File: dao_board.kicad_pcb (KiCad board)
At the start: 2 copper layers, 80 x 57 mm, 39 parts, among them J1 KEY1, J10 DISH_SENSOR, J11 5V_BOOST, J12 BATTERY, J13 DISH_LED, J2 KEY2, J3 KEY3, J4 KEY4, J5 KEY5, J6 KEY6, J7 KEY7, J8 START, J9 SELECT, SW1 SW_SPDT, SW2 HX 3x4x2-2P-1.6N, U1 XIAO-nRF52840-Plus-SMD, U2 74HC595, U3 74HC595

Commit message: 回路図を大幅に更新したのでPCBは作り直し
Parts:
- removed C1, C3, C4: 100n, PCM_Capacitor_SMD_AKL:C_0402_1005Metric
- removed C2: 10u, PCM_Capacitor_SMD_AKL:C_0603_1608Metric
- removed D1, D2: 1SS404, PCM_Diode_SMD_AKL:D_SOD-323
- removed H1, H2, H3, H4: MountingHole, PCM_fab:MountingHole_M5
- removed J1: KEY1, Connector_JST:JST_XH_B4B-XH-A_1x04_P2.50mm_Vertical
- removed J10: DISH_SENSOR, Connector_JST:JST_XH_B4B-XH-A_1x04_P2.50mm_Vertical
- removed J11: 5V_BOOST, Connector_JST:JST_XH_B4B-XH-A_1x04_P2.50mm_Vertical
- removed J12: BATTERY, Connector_JST:JST_PH_B2B-PH-K_1x02_P2.00mm_Vertical
- removed J13: DISH_LED, Connector_JST:JST_XH_B2B-XH-A_1x02_P2.50mm_Vertical
- removed J2: KEY2, Connector_JST:JST_XH_B4B-XH-A_1x04_P2.50mm_Vertical
- removed J3: KEY3, Connector_JST:JST_XH_B4B-XH-A_1x04_P2.50mm_Vertical
- removed J4: KEY4, Connector_JST:JST_XH_B4B-XH-A_1x04_P2.50mm_Vertical
- removed J5: KEY5, Connector_JST:JST_XH_B4B-XH-A_1x04_P2.50mm_Vertical
- removed J6: KEY6, Connector_JST:JST_XH_B4B-XH-A_1x04_P2.50mm_Vertical
- removed J7: KEY7, Connector_JST:JST_XH_B4B-XH-A_1x04_P2.50mm_Vertical
- removed J8: START, Connector_JST:JST_XH_B4B-XH-A_1x04_P2.50mm_Vertical
- removed J9: SELECT, Connector_JST:JST_XH_B4B-XH-A_1x04_P2.50mm_Vertical
- removed R1, R2: 1k, PCM_Resistor_SMD_AKL:R_0402_1005Metric
- removed R3, R4: 10k, PCM_Resistor_SMD_AKL:R_0402_1005Metric
- removed R5: 0, PCM_Resistor_SMD_AKL:R_0402_1005Metric
- removed SW1: SW_SPDT, IIDXtorollerparts:SW-SMD_MK-12C02-G020
- removed SW2: HX 3x4x2-2P-1.6N, IIDXtorollerparts:KEY-SMD_L4.0-W3.0-LS4.9-1
- removed TP1: SCR_5V, TestPoint:TestPoint_Pad_D2.0mm
- removed TP2: GND, TestPoint:TestPoint_Pad_D2.0mm
- removed TP3: RD1, TestPoint:TestPoint_Pad_D2.0mm
- removed TP4: RD2, TestPoint:TestPoint_Pad_D2.0mm
- removed TP5: VBUS_5V, TestPoint:TestPoint_Pad_D2.0mm
- removed TP6: 3V3, TestPoint:TestPoint_Pad_D2.0mm
- removed U1: XIAO-nRF52840-Plus-SMD, foot_one:XIAO-nRF52840-Plus-SMD
- removed U2, U3: 74HC595, PCM_Package_SO_AKL:TSSOP-16_4.4x5mm_P0.65mm
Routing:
- net GND: track 311.4 -> 0.00 mm, vias 4 -> 0
- net +3V3: track 140.7 -> 0.00 mm, vias 6 -> 0
- net /LED_CLK: track 86.6 -> 0.00 mm, vias 8 -> 0
- net /RD1: track 86.3 -> 0.00 mm, vias 2 -> 0
- net /K3: track 82.9 -> 0.00 mm, vias 1 -> 0
- net /RD2: track 81.5 -> 0.00 mm, vias 2 -> 0
- net /K7: track 72.3 -> 0.00 mm, vias 1 -> 0
- net /VBUS_5V: track 68.8 -> 0.00 mm, vias 4 -> 0
- net /BAT_SW: track 67.1 -> 0.00 mm, vias 5 -> 0
- net /K1: track 66.7 -> 0.00 mm, vias 1 -> 0
- net /K4: track 66.7 -> 0.00 mm, vias 1 -> 0
- net /LED_LATCH: track 60.9 -> 0.00 mm, vias 4 -> 0
- net /K5: track 60.2 -> 0.00 mm, vias 1 -> 0
- net /K2: track 58.5 -> 0.00 mm, vias 1 -> 0
- net /SCR_5V: track 53.4 -> 0.00 mm
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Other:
- board outline removed

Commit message: 回路図を元にPCBを更新、まだ仮置き
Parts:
- added C1: 100n, Library:C_0402_1005Metric, F.Cu at (45.2, 49.9)
- added C2: 4.7u, Library:C_0603_1608Metric, F.Cu at (45.1, 82.7)
- added C3: 100n, Library:C_0402_1005Metric, F.Cu at (45.2, 52.0)
- added C4: 100n, Library:C_0402_1005Metric, F.Cu at (45.2, 54.1)
- added C5: 4.7u, Library:C_0603_1608Metric, F.Cu at (45.1, 85.4)
- added C6: 100n, Library:C_0402_1005Metric, F.Cu at (45.2, 56.2)
- added D1: 1SS404, Library:D_SOD-323, F.Cu at (45.1, 88.7)
- added D2: SS14, Diode_SMD:D_SMA, F.Cu at (41.9, 78.3)
- added H1: MountingHole, Library:MountingHole_M5, F.Cu at (33.9, 36.1)
- added H2: MountingHole, Library:MountingHole_M5, F.Cu at (33.9, 42.4)
- added H3: MountingHole, Library:MountingHole_M5, F.Cu at (33.9, 48.7)
- added H4: MountingHole, Library:MountingHole_M5, F.Cu at (33.9, 55.0)
- added J1: DISH_LED, Library:JST_XH_B2B-XH-A_1x02_P2.50mm_Vertical, F.Cu at (40.5, 44.4)
- added J10: KEY6, Library:JST_XH_B4B-XH-A_1x04_P2.50mm_Vertical, F.Cu at (19.8, 57.8)
- added J11: KEY7, Library:JST_XH_B4B-XH-A_1x04_P2.50mm_Vertical, F.Cu at (19.8, 65.6)
- added J12: START, Library:JST_XH_B4B-XH-A_1x04_P2.50mm_Vertical, F.Cu at (19.8, 73.4)
- added J13: SELECT, Library:JST_XH_B4B-XH-A_1x04_P2.50mm_Vertical, F.Cu at (19.8, 81.2)
- added J14: DISH_SENSOR, Library:JST_XH_B4B-XH-A_1x04_P2.50mm_Vertical, F.Cu at (19.8, 89.0)
- added J3: SWD, Connector:FanPinHeader_1x04_P2.54mm_Vertical, F.Cu at (39.3, 36.7)
- added J4: GPIO_EXPANSION, Connector_PinHeader_2.54mm:PinHeader_2x05_P2.54mm_Vertical, F.Cu at (33.0, 68.9)
- added J5: KEY1, Library:JST_XH_B4B-XH-A_1x04_P2.50mm_Vertical, F.Cu at (19.8, 18.8)
- added J6: KEY2, Library:JST_XH_B4B-XH-A_1x04_P2.50mm_Vertical, F.Cu at (19.8, 26.6)
- added J7: KEY3, Library:JST_XH_B4B-XH-A_1x04_P2.50mm_Vertical, F.Cu at (19.8, 34.4)
- added J8: KEY4, Library:JST_XH_B4B-XH-A_1x04_P2.50mm_Vertical, F.Cu at (19.8, 42.2)
- added J9: KEY5, Library:JST_XH_B4B-XH-A_1x04_P2.50mm_Vertical, F.Cu at (19.8, 50.0)
- added R1: 0, Library:R_0402_1005Metric, F.Cu at (45.6, 16.5)
- added R2: 5.1k, Library:R_0402_1005Metric, F.Cu at (45.6, 18.6)
- added R3: 5.1k, Library:R_0402_1005Metric, F.Cu at (45.6, 20.7)
- added R4: 10k, Library:R_0402_1005Metric, F.Cu at (45.6, 22.8)
- added R5: 10k, Library:R_0402_1005Metric, F.Cu at (45.6, 24.9)
- added R6: 1k, Library:R_0402_1005Metric, F.Cu at (45.6, 27.1)
- added R7: 1k, Library:R_0402_1005Metric, F.Cu at (45.6, 29.2)
- added SW1: RESET, Library:KEY-SMD_L4.0-W3.0-LS4.9-1, F.Cu at (40.3, 50.9)
- added SW2: HX 3x4x2-2P-1.6N, Library:KEY-SMD_L4.0-W3.0-LS4.9-1, F.Cu at (40.3, 55.2)
- added TP1: SCR_5V, Library:TestPoint_Pad_D2.0mm, F.Cu at (32.8, 83.4)
- added TP2: GND, Library:TestPoint_Pad_D2.0mm, F.Cu at (32.8, 87.4)
- added TP3: RD1, Library:TestPoint_Pad_D2.0mm, F.Cu at (36.8, 83.4)
- added TP4: RD2, Library:TestPoint_Pad_D2.0mm, F.Cu at (36.8, 87.4)
- added TP5: VBUS_5V, Library:TestPoint_Pad_D2.0mm, F.Cu at (40.9, 83.4)
- added TP6: 3V3, Library:TestPoint_Pad_D2.0mm, F.Cu at (40.9, 87.4)
- added U1: MDBT50Q-1MV2, RF_Module:Raytac_MDBT50Q, F.Cu at (37.4, 24.2)
- added U2: TLC6C598PWR, c2863406:TSSOP-16_L5.0-W4.4-P0.65-LS6.4-BL, F.Cu at (34.4, 62.4)
- added U3: TLC6C598PWR, c2863406:TSSOP-16_L5.0-W4.4-P0.65-LS6.4-BL, F.Cu at (41.3, 62.4)
- added USBC1: TYPE-C-31-M-12, c165948:USB-C_SMD-TYPE-C-31-M-12_1, F.Cu at (43.3, 70.3)

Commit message: 主要部品を配置、ここから位置整理を開始
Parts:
- moved J5 193.5 mm to (159.3, 152.9)
- moved TP2 177.8 mm to (195.8, 158.4)
- moved TP6 177.3 mm to (203.6, 157.9)
- moved TP4 177.3 mm to (199.3, 158.4)
- moved TP1 176.7 mm to (195.5, 152.3)
- moved TP3 176.7 mm to (199.5, 152.3)
- moved TP5 176.7 mm to (203.6, 152.3)
- moved J6 176.6 mm to (151.3, 144.4)
- moved J7 171.6 mm to (143.8, 152.9)
- moved H4 167.8 mm to (175.5, 145.0), turned to 180 degrees
- moved H2 159.1 mm to (175.5, 115.0), turned to 180 degrees
- moved J8 154.6 mm to (135.8, 144.4)
- moved J13 151.2 mm to (169.3, 103.4)
- moved J9 149.6 mm to (128.3, 152.9)
- moved R2 148.0 mm to (160.8, 111.5), turned to 90 degrees
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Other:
- board outline added: 80 x 57 mm
- board text added: "3V3"
- board text added: "CLK"
- board text added: "GND"
- board text added: "IO"

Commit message: 基盤内に部品を収めることに成功、これから配線ルールの設定をする
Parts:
- moved TP1 87.6 mm to (112.8, 123.4)
- moved TP2 86.4 mm to (116.8, 123.4)
- moved TP6 74.3 mm to (136.3, 126.4)
- moved TP4 67.6 mm to (139.8, 126.4)
- moved TP3 61.9 mm to (143.3, 126.4)
- moved TP5 54.7 mm to (167.3, 111.4)
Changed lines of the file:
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@@
 	(footprint "Library:TestPoint_Pad_D2.0mm"
 		(layer "F.Cu")
-		(at 203.5761 157.8936)
+		(at 136.2861 126.3936)
 		(descr "SMD pad as test Point, diameter 2.0mm")
 		(tags "test point SMD pad")
@@
 	(footprint "Library:TestPoint_Pad_D2.0mm"
 		(layer "F.Cu")
-		(at 199.2861 158.3936)
+		(at 139.7861 126.3936)
 		(descr "SMD pad as test Point, diameter 2.0mm")
 		(tags "test point SMD pad")
@@
 	(footprint "Library:TestPoint_Pad_D2.0mm"
 		(layer "F.Cu")
-		(at 199.5261 152.2936)
+		(at 143.2861 126.3936)
 		(descr "SMD pad as test Point, diameter 2.0mm")
 		(tags "test point SMD pad")
@@
 	(footprint "Library:TestPoint_Pad_D2.0mm"
 		(layer "F.Cu")
-		(at 195.4761 152.2936)
+		(at 112.7861 123.3936)
 		(descr "SMD pad as test Point, diameter 2.0mm")
 		(tags "test point SMD pad")
@@
 	(footprint "Library:TestPoint_Pad_D2.0mm"
 		(layer "F.Cu")
-		(at 195.7861 158.3936)
+		(at 116.7861 123.3936)
 		(descr "SMD pad as test Point, diameter 2.0mm")
 		(tags "test point SMD pad")
@@
 		)
 		(property "Value" "HX 3x4x2-2P-1.6N"
-			(at 0 -6 90)
+			(at -4 -1 180)
 			(layer "F.Fab")
 			(effects
@@
 	(footprint "Library:C_0603_1608Metric"
 		(layer "F.Cu")
-		(at 121.8061 130.3936)
+		(at 121.7861 130.3936)
 		(descr "Capacitor SMD 0603 (1608 Metric), square (rectangular) end terminal, IPC_7351 nominal, (Body size source: IPC-SM-782 page 76, https://www.pcb-3d.com/wordpress/wp-content/uploads/ipc-sm-782a_amendment_1_and_2.pdf), Alternate KiCad Library")
 		(tags "capacitor")
@@
 	(footprint "Library:TestPoint_Pad_D2.0mm"
 		(layer "F.Cu")
-		(at 203.5761 152.2936)
+		(at 167.2861 111.3936)
 		(descr "SMD pad as test Point, diameter 2.0mm")
 		(tags "test point SMD pad")

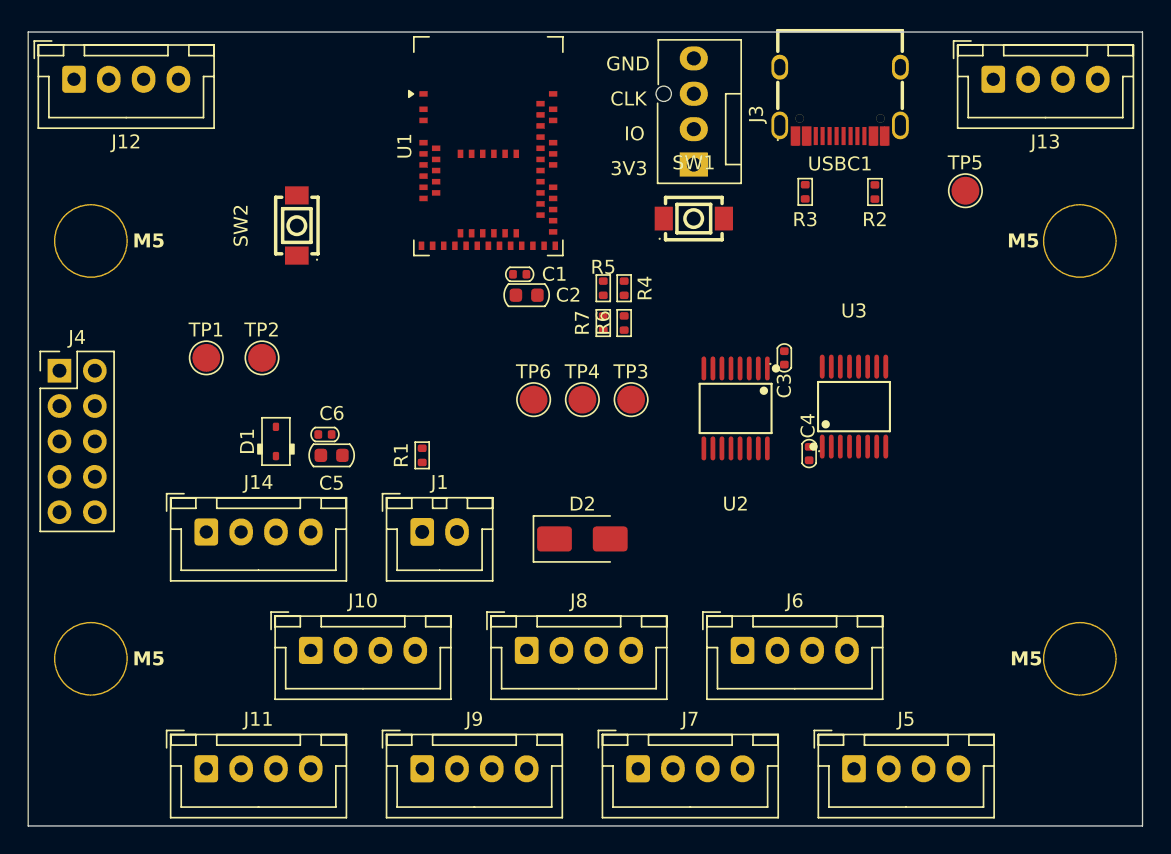
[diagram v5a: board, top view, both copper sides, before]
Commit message: 途中まで配線、あとなぜかマイコンにVBUSを接続してなかったので回路図側は修正
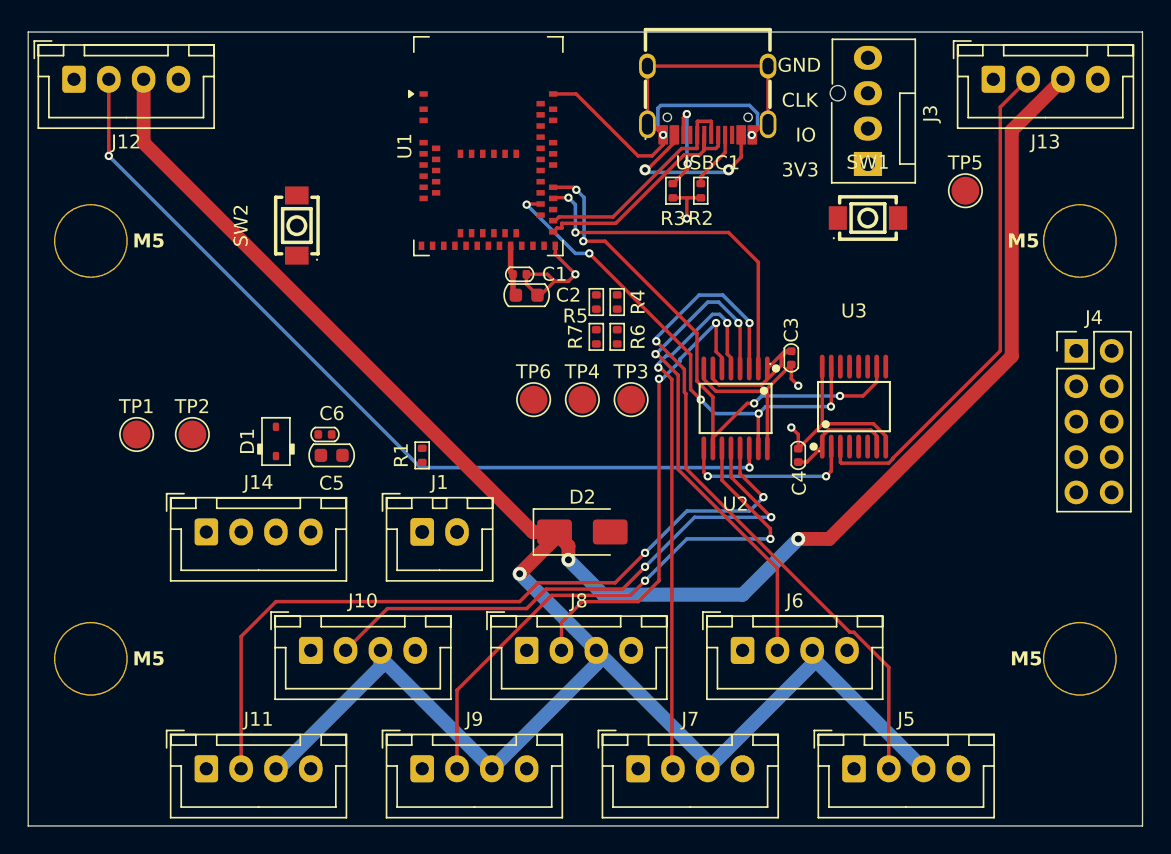
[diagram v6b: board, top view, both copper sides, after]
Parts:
- moved J4 73.0 mm to (175.2, 122.9)
- moved R2 12.5 mm to (148.3, 111.4)
- moved J3 12.5 mm to (160.3, 109.5)
- moved SW1 12.5 mm to (160.3, 113.4)
- moved R3 9.50 mm to (146.3, 111.4)
- moved USBC1 9.50 mm to (148.8, 104.9)
- moved TP1 7.43 mm to (107.8, 128.9)
- moved TP2 7.43 mm to (111.8, 128.9)
- moved R4 1.11 mm to (140.8, 119.4)
- moved R5 1.11 mm to (142.3, 119.4)
- moved R6 1.11 mm to (142.3, 121.9)
- moved R7 1.11 mm to (140.8, 121.9)
- moved C4 0.79 mm to (155.3, 130.4), turned to -90 degrees
- moved C3 0.50 mm to (154.8, 123.4), turned to 90 degrees
- moved D2 0.50 mm to (139.8, 135.9)
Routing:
- net /KEY_LED_5V: track 0.00 -> 191.6 mm, vias 0 -> 3
- net GND: track 0.00 -> 83.8 mm, vias 0 -> 6
- net /LED_K8: track 0.00 -> 62.2 mm, vias 0 -> 2
- net /LED_K7: track 0.00 -> 55.3 mm, vias 0 -> 2
- net /LED_K1: track 0.00 -> 50.1 mm, vias 0 -> 2
- net /LED_K6: track 0.00 -> 40.7 mm, vias 0 -> 2
- net /LED_LATCH: track 0.00 -> 40.6 mm, vias 0 -> 4
- net /LED_K5: track 0.00 -> 40.6 mm, vias 0 -> 2
- net /LED_K3: track 0.00 -> 39.7 mm, vias 0 -> 2
- net /LED_K2: track 0.00 -> 36.4 mm, vias 0 -> 2
- net /LED_K9: track 0.00 -> 36.3 mm
- net /LED_CLK: track 0.00 -> 36.1 mm, vias 0 -> 5
- net /LED_K4: track 0.00 -> 34.0 mm, vias 0 -> 2
- net /VBUS_5V: track 0.00 -> 30.6 mm, vias 0 -> 2
- net /LED_DATA: track 0.00 -> 25.5 mm, vias 0 -> 2
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
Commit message: 配線途中のコミット
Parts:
- moved TP5 8.75 mm to (162.8, 118.9)
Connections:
- U1 pad 30: unconnected-(U1-VDDH-Pad30) -> /VBUS_5V
- U1 pad 32: unconnected-(U1-VBUS-Pad32) -> /VBUS_5V
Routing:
- net /VBUS_5V: track 30.6 -> 141.5 mm, vias 2 -> 10

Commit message: 配線スパゲッティ過ぎてこれもうわかんねぇな
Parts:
- moved SW1 12.9 mm to (147.8, 116.4)
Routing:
- net /K1: track 0.00 -> 119.0 mm, vias 0 -> 2
- net /K3: track 0.00 -> 100.2 mm, vias 0 -> 2
- net /K5: track 0.00 -> 87.6 mm, vias 0 -> 3
- net /K4: track 0.00 -> 83.3 mm, vias 0 -> 7
- net +3V3: track 3.70 -> 79.5 mm, vias 0 -> 6
- net /K6: track 0.00 -> 67.2 mm, vias 0 -> 3
- net /K7: track 0.00 -> 64.6 mm, vias 0 -> 3
- net /SELECT: track 0.00 -> 54.5 mm, vias 0 -> 4
- net Net-(J14-Pin_1): track 0.00 -> 45.4 mm, vias 0 -> 4
- net /K2: track 0.00 -> 44.9 mm, vias 0 -> 4
- net Net-(J14-Pin_2): track 0.00 -> 38.8 mm, vias 0 -> 6
- net /START: track 0.00 -> 31.7 mm, vias 0 -> 1
- net /RD1: track 0.00 -> 24.4 mm, vias 0 -> 6
- net /RD2: track 0.00 -> 22.5 mm, vias 0 -> 4
- net /MODE_PAIR: track 0.00 -> 16.5 mm, vias 0 -> 2
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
